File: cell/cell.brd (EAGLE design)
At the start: 35.6 x 48.3 mm, 11 parts

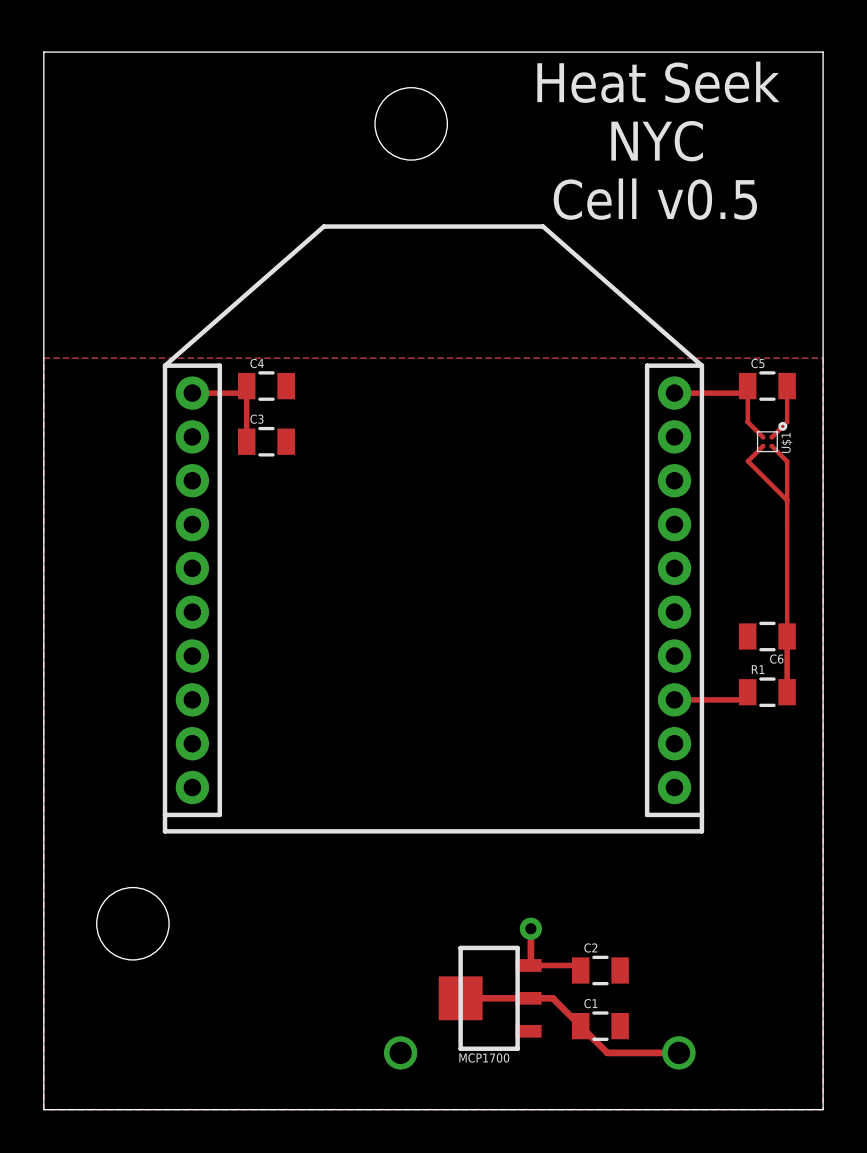
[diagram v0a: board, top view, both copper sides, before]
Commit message: Doodles from @raphaelabrams - simplified the power supply rail to a star - strengthened the ground plane - added several decoupling capacitors
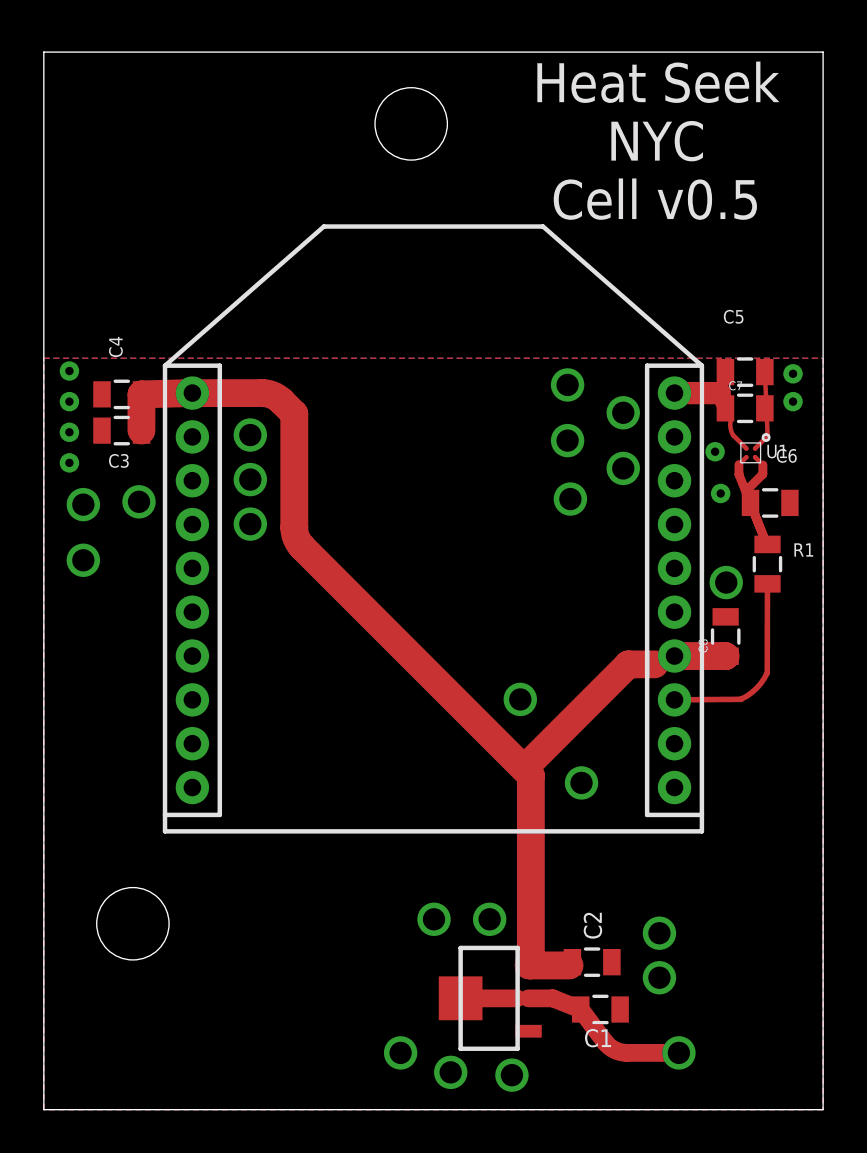
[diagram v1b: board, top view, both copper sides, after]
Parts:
- removed U$1: LMT70, lmt70:YFP0004
- added C7: 0.1µF, SparkFun-Capacitors:0805
- added C8: 1µF, SparkFun-Capacitors:0805
- added U1: LMT70, lmt70:YFP0004
- moved C3 6.62 mm to (3.56, 31.0), turned to 180 degrees
- moved C4 6.61 mm to (3.56, 32.6), turned to 180 degrees
- moved C6 6.10 mm to (33.1, 27.7), turned to 0 degrees
- moved R1 5.84 mm to (33.0, 24.9), turned to 90 degrees
- moved C5 1.20 mm to (32.0, 33.7)
- moved C1 0.76 mm to (25.4, 4.57)
- moved C2 0.54 mm to (25.0, 6.73)
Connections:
- net 3.3V: now also C8.1
- net GND: now also C7.2, C8.2, U1.GND; no longer U$1.GND
- net N$1: now also U1.T_ON, U1.VDD; no longer U$1.T_ON, U$1.VDD
- net N$7: now also C7.1, U1.TAO; no longer U$1.TAO
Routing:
- net 3.3V: track 9.73 -> 52.2 mm, vias 1 -> 0
- net N$2: track 3.69 -> 8.79 mm
- net N$1: track 15.1 -> 10.8 mm
- net GND: track 2.63 -> 3.72 mm, vias 1 -> 29
- net N$7: track 5.97 -> 6.92 mm
- added copper zone on layer 16, net GND
- removed copper zone on layer 16, net 3.3V
